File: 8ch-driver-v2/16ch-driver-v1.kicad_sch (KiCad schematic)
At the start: 5 parts, among them J1 Barrel_Jack

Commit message: push
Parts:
- added J2: Conn_02x16_Odd_Even, Connector_PinHeader_2.54mm:PinHeader_2x16_P2.54mm_Vertical, symbol Connector_Generic:Conn_02x16_Odd_Even
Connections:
- net GND: now also J2.10 (Pin_10), J2.12 (Pin_12), J2.14 (Pin_14), J2.16 (Pin_16), J2.18 (Pin_18), J2.2 (Pin_2), J2.20 (Pin_20), J2.22 (Pin_22), J2.24 (Pin_24), J2.26 (Pin_26), J2.28 (Pin_28), J2.30 (Pin_30), J2.32 (Pin_32), J2.4 (Pin_4), J2.6 (Pin_6), J2.8 (Pin_8)
- net SpikeAndHoldDriverAndLEDs-1/DriveOut: now also J2.1 (Pin_1)
- net SpikeAndHoldDriverAndLEDs-10/DriveOut: now also J2.19 (Pin_19)
- net SpikeAndHoldDriverAndLEDs-11/DriveOut: now also J2.21 (Pin_21)
- net SpikeAndHoldDriverAndLEDs-12/DriveOut: now also J2.23 (Pin_23)
- net SpikeAndHoldDriverAndLEDs-13/DriveOut: now also J2.25 (Pin_25)
- net SpikeAndHoldDriverAndLEDs-14/DriveOut: now also J2.27 (Pin_27)
- net SpikeAndHoldDriverAndLEDs-15/DriveOut: now also J2.29 (Pin_29)
- net SpikeAndHoldDriverAndLEDs-16/DriveOut: now also J2.31 (Pin_31)
- net SpikeAndHoldDriverAndLEDs-2/DriveOut: now also J2.3 (Pin_3)
- net SpikeAndHoldDriverAndLEDs-3/DriveOut: now also J2.5 (Pin_5)
- net SpikeAndHoldDriverAndLEDs-4/DriveOut: now also J2.7 (Pin_7)
- net SpikeAndHoldDriverAndLEDs-5/DriveOut: now also J2.9 (Pin_9)
- net SpikeAndHoldDriverAndLEDs-6/DriveOut: now also J2.11 (Pin_11)
- net SpikeAndHoldDriverAndLEDs-7/DriveOut: now also J2.13 (Pin_13)
- net SpikeAndHoldDriverAndLEDs-8/DriveOut: now also J2.15 (Pin_15)
- net SpikeAndHoldDriverAndLEDs-9/DriveOut: now also J2.17 (Pin_17)
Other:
- note removed: "DRIVER6 ACTIVE LIGHT"

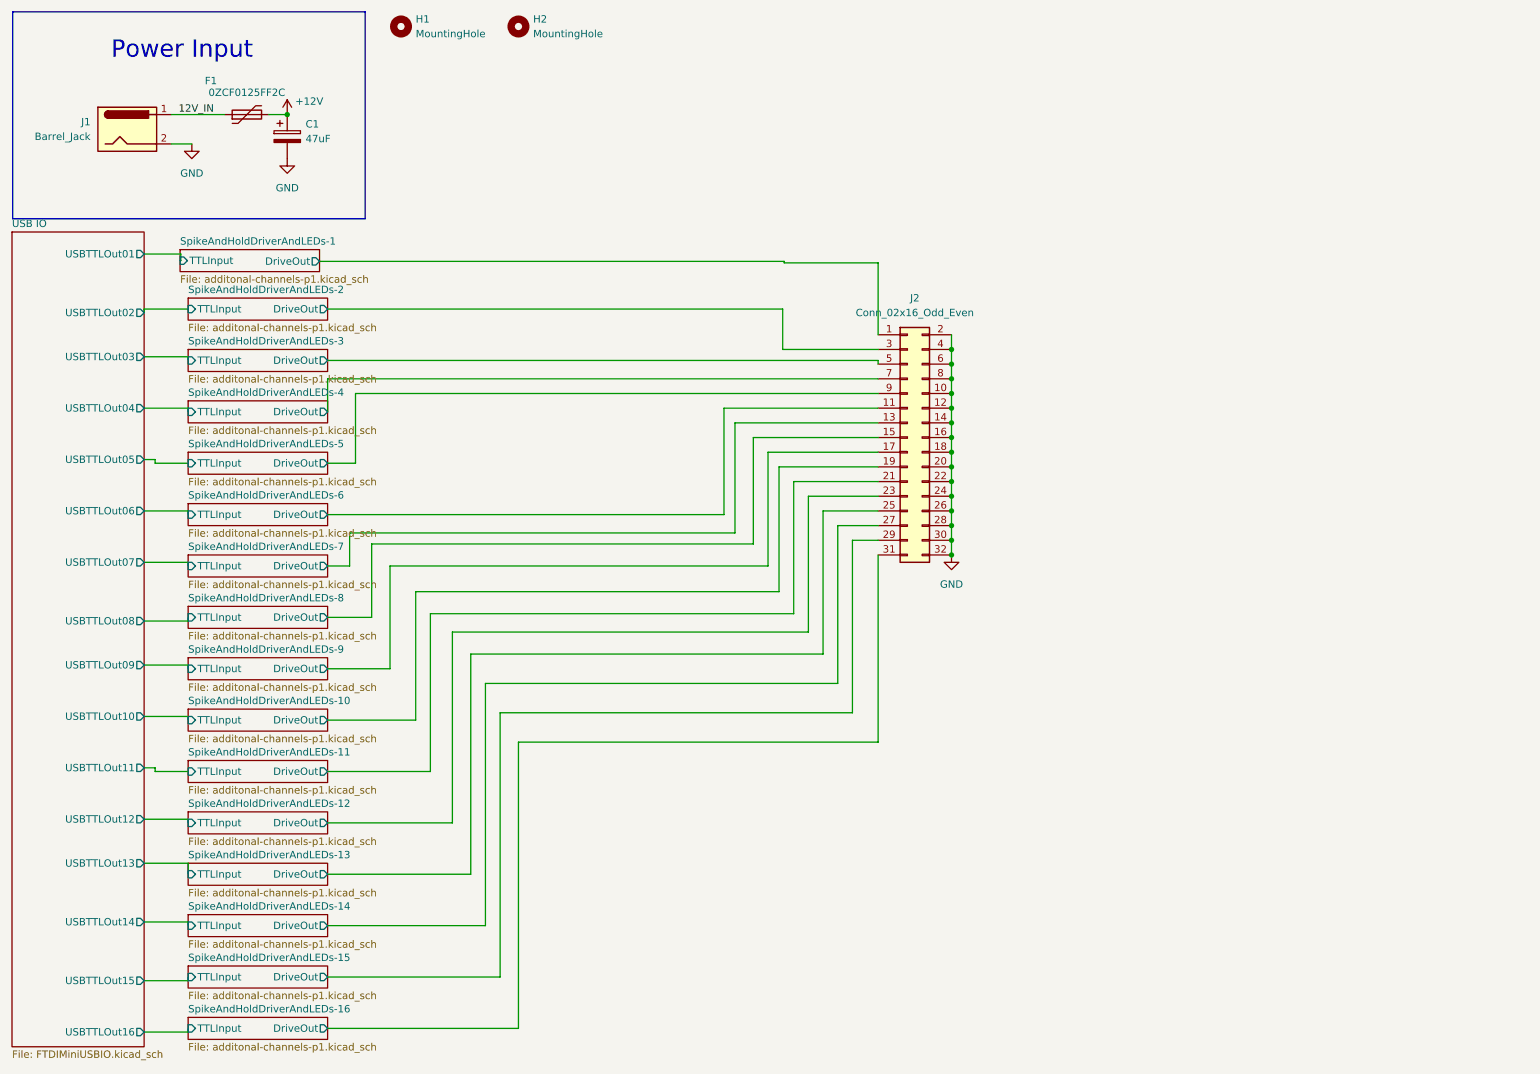
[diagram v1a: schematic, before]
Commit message: 16-valve PCB layout for inspection
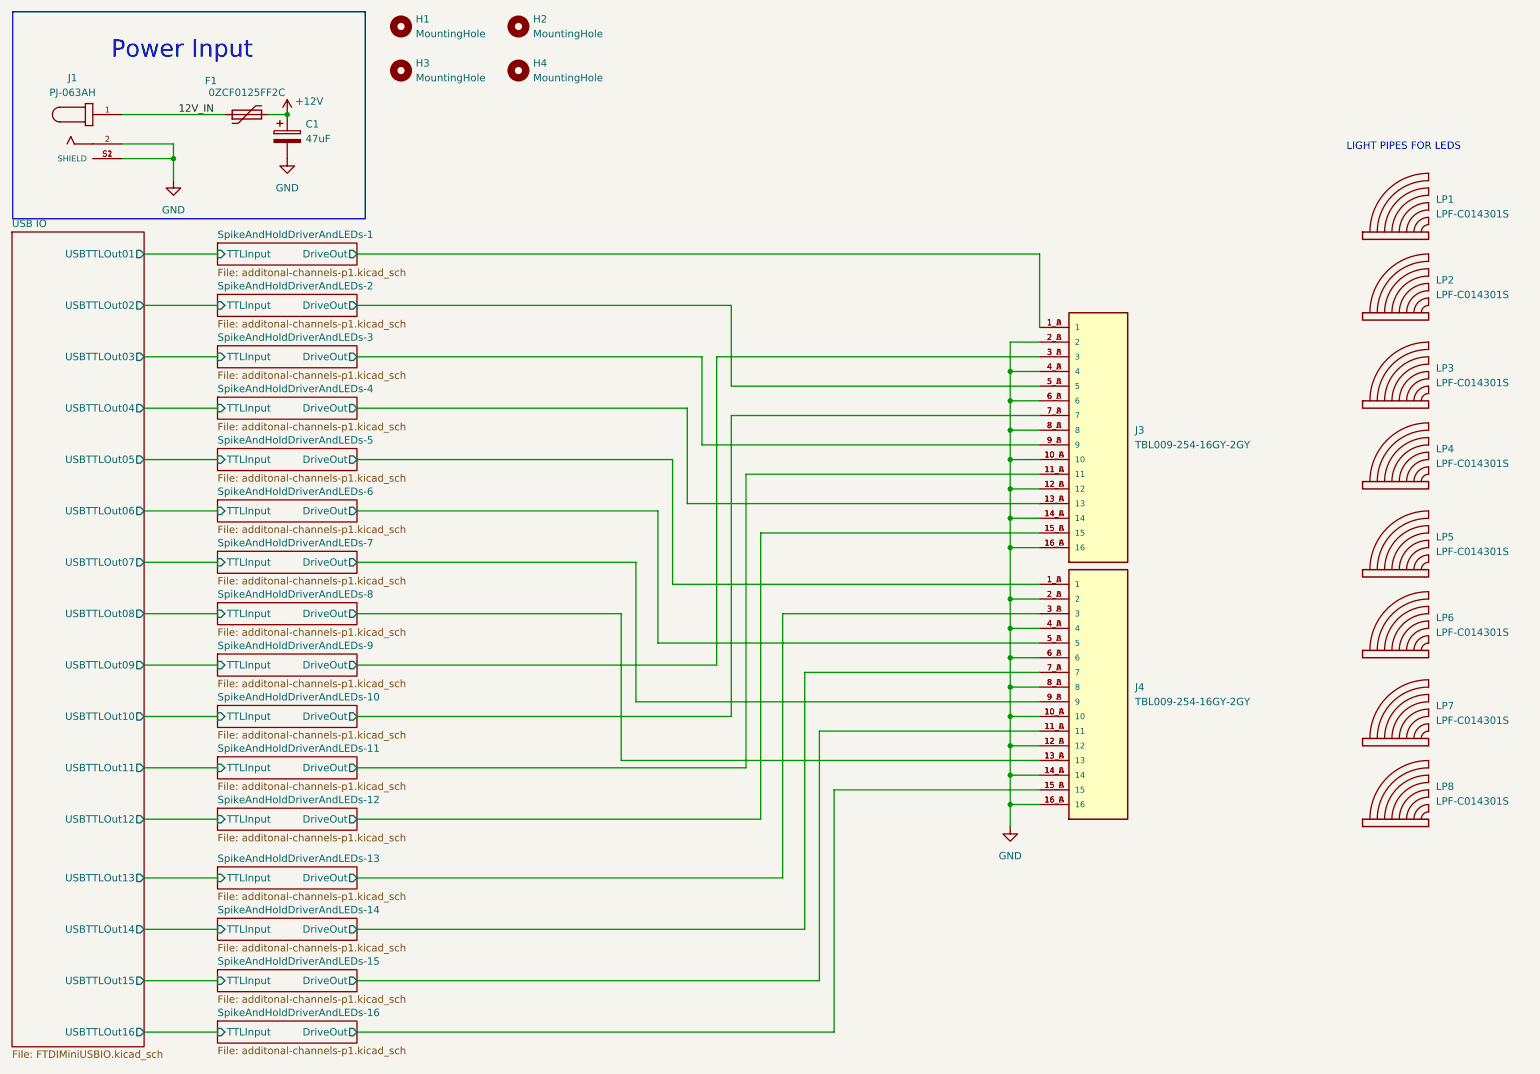
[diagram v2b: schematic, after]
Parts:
- removed J1: Barrel_Jack, Connector_BarrelJack:BarrelJack_CUI_PJ-063AH_Horizontal, symbol Connector:Barrel_Jack
- removed J2: Conn_02x16_Odd_Even, Connector_PinHeader_2.54mm:PinHeader_2x16_P2.54mm_Vertical, symbol Connector_Generic:Conn_02x16_Odd_Even
- added H3, H4: MountingHole, MountingHole:MountingHole_3.2mm_M3, symbol Mechanical:MountingHole
- added J1: PJ-063AH, footprint:CUI_PJ-063AH, symbol PJ-063AH:PJ-063AH
- added J3, J4: TBL009-254-16GY-2GY, footprint:CUI_TBL009-254-16GY-2GY, symbol TBL009-254-16GY-2GY:TBL009-254-16GY-2GY
- added LP1, LP2, LP3, LP4, LP5, LP6, LP7, LP8: LPF-C014301S, footprint:Lightpipe_LPF-C014301S, symbol LPF-C014301S:LPF-C014301S
- H1, H2: footprint MountingHole:MountingHole_2.2mm_M2_Pad -> MountingHole:MountingHole_3.2mm_M3
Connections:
- net 12V_IN: now also J1.1
- net GND: now also J1.2, J1.S1 (SHIELD), J1.S2 (SHIELD), J3.10_A (10), J3.10_B (10), J3.12_A (12), J3.12_B (12), J3.14_A (14), J3.14_B (14), J3.16_A (16), J3.16_B (16), J3.2_A (2), J3.2_B (2), J3.4_A (4), J3.4_B (4), J3.6_A (6), J3.6_B (6), J3.8_A (8), J3.8_B (8), J4.10_A (10), J4.10_B (10), J4.12_A (12), J4.12_B (12), J4.14_A (14), J4.14_B (14), J4.16_A (16), J4.16_B (16), J4.2_A (2), J4.2_B (2), J4.4_A (4), J4.4_B (4), J4.6_A (6), J4.6_B (6), J4.8_A (8), J4.8_B (8)
- net SpikeAndHoldDriverAndLEDs-1/DriveOut: now also J3.1_A (1), J3.1_B (1)
- net SpikeAndHoldDriverAndLEDs-10/DriveOut: now also J3.7_A (7), J3.7_B (7)
- net SpikeAndHoldDriverAndLEDs-11/DriveOut: now also J3.11_A (11), J3.11_B (11)
- net SpikeAndHoldDriverAndLEDs-12/DriveOut: now also J3.15_A (15), J3.15_B (15)
- net SpikeAndHoldDriverAndLEDs-13/DriveOut: now also J4.3_A (3), J4.3_B (3)
- net SpikeAndHoldDriverAndLEDs-14/DriveOut: now also J4.7_A (7), J4.7_B (7)
- net SpikeAndHoldDriverAndLEDs-15/DriveOut: now also J4.11_A (11), J4.11_B (11)
- net SpikeAndHoldDriverAndLEDs-16/DriveOut: now also J4.15_A (15), J4.15_B (15)
- net SpikeAndHoldDriverAndLEDs-2/DriveOut: now also J3.5_A (5), J3.5_B (5)
- net SpikeAndHoldDriverAndLEDs-3/DriveOut: now also J3.9_A (9), J3.9_B (9)
- net SpikeAndHoldDriverAndLEDs-4/DriveOut: now also J3.13_A (13), J3.13_B (13)
- net SpikeAndHoldDriverAndLEDs-5/DriveOut: now also J4.1_A (1), J4.1_B (1)
- net SpikeAndHoldDriverAndLEDs-6/DriveOut: now also J4.5_A (5), J4.5_B (5)
- net SpikeAndHoldDriverAndLEDs-7/DriveOut: now also J4.9_A (9), J4.9_B (9)
- net SpikeAndHoldDriverAndLEDs-8/DriveOut: now also J4.13_A (13), J4.13_B (13)
- net SpikeAndHoldDriverAndLEDs-9/DriveOut: now also J3.3_A (3), J3.3_B (3)
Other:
- note added: "LIGHT PIPES FOR LEDS"
- company: Boston University -> BU EDF
